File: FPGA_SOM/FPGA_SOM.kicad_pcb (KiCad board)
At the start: 6 copper layers, 42 x 38 mm, 47 parts, among them J102 Conn_01x14, J103 Conn_01x09, J104 Conn_01x11, J105 Conn_01x02, J106 Conn_01x06, U102 AP2127N-3.3, U103 W25X20CLSN, U104 AP2127N-1.2, U105 ICE40UP5K-SG48ITR, X101 ECS-2520MV-xxx-xx

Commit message: First attempt at V2. Likely to be changed in the near future.
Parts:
- removed C101, C103, C111, C123, C124, C125, C138: 100n, Capacitor_SMD:C_0603_1608Metric_Pad1.08x0.95mm_HandSolder
- removed C102, C105, C114, C126, C127, C136: 10n, Capacitor_SMD:C_0603_1608Metric_Pad1.08x0.95mm_HandSolder
- removed C116, C119, C122, C128, C137: 10u, Capacitor_SMD:C_0603_1608Metric_Pad1.08x0.95mm_HandSolder
- removed C134: 22u, Capacitor_SMD:C_0603_1608Metric_Pad1.08x0.95mm_HandSolder
- removed D101, D102, D103: LED, Diode_SMD:D_0603_1608Metric_Pad1.05x0.95mm_HandSolder
- removed D104: 1N4004, Diode_SMD:D_0603_1608Metric_Pad1.05x0.95mm_HandSolder
- removed D105, D106, D108: LED_Small, Diode_SMD:D_0603_1608Metric_Pad1.05x0.95mm_HandSolder
- removed FB101: FerriteBead, Resistor_SMD:R_1206_3216Metric
- removed J102: Conn_01x14, Connector_PinHeader_2.54mm:PinHeader_1x14_P2.54mm_Vertical
- removed J103: Conn_01x09, Connector_PinHeader_2.54mm:PinHeader_1x09_P2.54mm_Vertical
- removed J104: Conn_01x11, Connector_PinHeader_2.54mm:PinHeader_1x11_P2.54mm_Vertical
- removed J105: Conn_01x02, Connector_PinHeader_2.54mm:PinHeader_1x02_P2.54mm_Vertical
- removed J106: Conn_01x06, Connector_PinHeader_2.54mm:PinHeader_1x06_P2.54mm_Vertical
- removed R105: 100, Resistor_SMD:R_0603_1608Metric_Pad0.98x0.95mm_HandSolder
- removed R106, R109: 2k2, Resistor_SMD:R_0603_1608Metric_Pad0.98x0.95mm_HandSolder
- removed R107, R108, R111, R114: 1k, Resistor_SMD:R_0603_1608Metric_Pad0.98x0.95mm_HandSolder
- removed R110: 5k, Resistor_SMD:R_0603_1608Metric_Pad0.98x0.95mm_HandSolder
- removed R112, R113: 10k, Resistor_SMD:R_0603_1608Metric_Pad0.98x0.95mm_HandSolder
- removed U102: AP2127N-3.3, Package_TO_SOT_SMD:SOT-23
- removed U103: W25X20CLSN, Package_SO:SOIC-8_3.9x4.9mm_P1.27mm
- removed U104: AP2127N-1.2, Package_TO_SOT_SMD:SOT-23
- removed U105: ICE40UP5K-SG48ITR, Package_DFN_QFN:QFN-48-1EP_7x7mm_P0.5mm_EP5.6x5.6mm
- removed X101: ECS-2520MV-xxx-xx, Oscillator:Oscillator_SMD_ECS_2520MV-xxx-xx-4Pin_2.5x2.0mm
- added ?: VPP, TestPoint:TestPoint_Pad_2.0x2.0mm, F.Cu at (131.6, 134.6)
- added C1: 100n, Capacitor_SMD:C_0603_1608Metric, F.Cu at (131.7, 122.3)
- added C10: 100n, Capacitor_SMD:C_0603_1608Metric, F.Cu at (131.8, 130.3)
- added C11: 100n, Capacitor_SMD:C_0603_1608Metric, F.Cu at (131.8, 126.8)
- added C12: 100n, Capacitor_SMD:C_0603_1608Metric, F.Cu at (118.6, 125.2)
- added C13: 10n, Capacitor_SMD:C_0603_1608Metric, F.Cu at (131.8, 125.3)
- added C14: 10n, Capacitor_SMD:C_0603_1608Metric, F.Cu at (118.6, 123.8)
- added C15: 10u, Capacitor_SMD:C_0805_2012Metric, F.Cu at (114.5, 114.5)
- added C16: 22u, Capacitor_SMD:C_0805_2012Metric, F.Cu at (108.6, 114.5)
- added C17: 10u, Capacitor_SMD:C_0805_2012Metric, F.Cu at (125.2, 112.4)
- added C18: 100n, Capacitor_SMD:C_0603_1608Metric, F.Cu at (125.0, 114.2)
- added C19: 10n, Capacitor_SMD:C_0603_1608Metric, F.Cu at (125.0, 115.7)
- added C2: 10n, Capacitor_SMD:C_0603_1608Metric, F.Cu at (131.7, 123.8)
- added C20: 100n, Capacitor_SMD:C_0603_1608Metric, F.Cu at (123.8, 131.3)
- added C3: 100n, Capacitor_SMD:C_0603_1608Metric, F.Cu at (125.5, 131.3)
- added C4: 10n, Capacitor_SMD:C_0603_1608Metric, F.Cu at (127.0, 131.3)
- added C5: 100n, Capacitor_SMD:C_0603_1608Metric, F.Cu at (118.6, 120.8)
- added C6: 10n, Capacitor_SMD:C_0603_1608Metric, F.Cu at (118.6, 122.3)
- added C7: 10u, Capacitor_SMD:C_0805_2012Metric, F.Cu at (114.6, 108.9)
- added C8: 10u, Capacitor_SMD:C_0805_2012Metric, F.Cu at (131.9, 128.5)
- added C9: 10u, Capacitor_SMD:C_0805_2012Metric, F.Cu at (108.7, 108.9)
- added D1: 1N4004, Diode_SMD:D_0603_1608Metric, F.Cu at (128.7, 131.3)
- added D2: LED_Small, Diode_SMD:D_0603_1608Metric_Pad1.05x0.95mm_HandSolder, F.Cu at (135.9, 111.6)
- added D3: LED_Small, Diode_SMD:D_0603_1608Metric_Pad1.05x0.95mm_HandSolder, F.Cu at (135.9, 114.5)
- added D4: LED_Small, Diode_SMD:D_0603_1608Metric_Pad1.05x0.95mm_HandSolder, F.Cu at (135.9, 117.5)
- added D5: LED, Diode_SMD:D_0603_1608Metric, F.Cu at (110.9, 118.7)
- added D6: LED, Diode_SMD:D_0603_1608Metric, F.Cu at (110.9, 121.7)
- added D7: LED, Diode_SMD:D_0603_1608Metric, F.Cu at (113.0, 128.2)
- added FB1: FerriteBead, Resistor_SMD:R_1206_3216Metric, F.Cu at (125.7, 110.3)
- added J1: Conn_01x14, Connector_PinHeader_2.54mm:PinHeader_1x14_P2.54mm_Vertical, F.Cu at (147.3, 142.2)
- added J2: Conn_01x09, Connector_PinHeader_2.54mm:PinHeader_1x09_P2.54mm_Vertical, F.Cu at (134.6, 101.6)
- added J3: Conn_01x11, Connector_PinHeader_2.54mm:PinHeader_1x11_P2.54mm_Vertical, F.Cu at (116.8, 147.3)
- added J4: Conn_01x04, Connector_PinHeader_2.54mm:PinHeader_1x04_P2.54mm_Vertical, F.Cu at (104.1, 101.6)
- added J5: Conn_01x02, Connector_PinHeader_2.54mm:PinHeader_1x02_P2.54mm_Vertical, F.Cu at (113.7, 131.6)
- added J6: Conn_02x04_Counter_Clockwise, Connector_PinHeader_2.54mm:PinHeader_2x04_P2.54mm_Vertical, F.Cu at (111.8, 144.8)
- added R1: 100, Resistor_SMD:R_0603_1608Metric, F.Cu at (131.9, 131.8)
- added R10: 10k, Resistor_SMD:R_0603_1608Metric, F.Cu at (126.0, 135.3)
- added R11: 0, Resistor_SMD:R_0603_1608Metric, F.Cu at (108.7, 141.5)
- added R12: 0, Resistor_SMD:R_0603_1608Metric, F.Cu at (107.2, 141.4)
- added R2: 2k2, Resistor_SMD:R_0603_1608Metric, F.Cu at (113.9, 118.7)
- added R3: 1k, Resistor_SMD:R_0603_1608Metric, F.Cu at (132.8, 111.6)
- added R4: 1k, Resistor_SMD:R_0603_1608Metric, F.Cu at (132.8, 114.5)
- added R5: 1k, Resistor_SMD:R_0603_1608Metric, F.Cu at (132.8, 117.5)
- added R6: 1k, Resistor_SMD:R_0603_1608Metric, F.Cu at (113.9, 121.7)
- added R7: 2k2, Resistor_SMD:R_0603_1608Metric, F.Cu at (116.0, 128.2)
- added R8: 4k7, Resistor_SMD:R_0603_1608Metric, F.Cu at (116.0, 126.7)
- added R9: 10k, Resistor_SMD:R_0603_1608Metric, F.Cu at (111.2, 133.4)
- added TP10: ~{RST}, TestPoint:TestPoint_Pad_2.0x2.0mm, F.Cu at (108.3, 125.9)
- added TP11: CDN, TestPoint:TestPoint_Pad_2.0x2.0mm, F.Cu at (112.8, 124.5)
- added TP12: OSC, TestPoint:TestPoint_Pad_2.0x2.0mm, F.Cu at (134.4, 105.8)
- added TP2: VPLL, TestPoint:TestPoint_Pad_2.0x2.0mm, F.Cu at (134.7, 134.6)
- added TP3: 3V3, TestPoint:TestPoint_Pad_2.0x2.0mm, F.Cu at (142.5, 103.1)
- added TP4: 1V2, TestPoint:TestPoint_Pad_2.0x2.0mm, F.Cu at (145.5, 103.0)
- added TP5: FSS, TestPoint:TestPoint_Pad_2.0x2.0mm, F.Cu at (108.3, 134.3)
- added TP6: ISS, TestPoint:TestPoint_Pad_2.0x2.0mm, F.Cu at (108.3, 130.2)
- added TP7: SCK, TestPoint:TestPoint_Pad_2.0x2.0mm, F.Cu at (103.5, 141.2)
- added TP8: SDO, TestPoint:TestPoint_Pad_2.0x2.0mm, F.Cu at (115.3, 138.3)
- added TP9: SDI, TestPoint:TestPoint_Pad_2.0x2.0mm, F.Cu at (111.4, 138.4)
- added U1: ICE40UP5K-SG48ITR, Package_DFN_QFN:QFN-48-1EP_7x7mm_P0.5mm_EP5.6x5.6mm, F.Cu at (125.0, 125.0)
- added U2: AP2127N-3.3, Package_TO_SOT_SMD:SOT-23, F.Cu at (111.6, 108.9)
- added U3: AP2127N-1.2, Package_TO_SOT_SMD:SOT-23, F.Cu at (111.6, 114.5)
- added U4: W25X20CLSN, Package_SO:SOIC-8_3.9x4.9mm_P1.27mm, F.Cu at (119.3, 132.9)
- added X1: ECS-2520MV-xxx-xx, Oscillator:Oscillator_SMD_ECS_2520MV-xxx-xx-4Pin_2.5x2.0mm, F.Cu at (125.2, 117.9)
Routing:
- net Net-(J104-Pin_2): track 33.0 -> 0.00 mm, vias 1 -> 0
- net Net-(J104-Pin_10): track 31.2 -> 0.00 mm, vias 1 -> 0
- net Net-(J104-Pin_1): track 30.0 -> 0.00 mm
- net Net-(J104-Pin_9): track 29.9 -> 0.00 mm, vias 1 -> 0
- net Net-(J1-Pin_14): track 0.00 -> 29.4 mm, vias 0 -> 1
- net Net-(J1-Pin_1): track 0.00 -> 27.5 mm, vias 0 -> 1
- net Net-(J1-Pin_13): track 0.00 -> 26.7 mm, vias 0 -> 1
- net Net-(J104-Pin_7): track 26.6 -> 0.00 mm, vias 1 -> 0
- net Net-(J102-Pin_14): track 26.2 -> 0.00 mm
- net Net-(J3-Pin_11): track 0.00 -> 26.0 mm, vias 0 -> 1
- net Net-(J2-Pin_8): track 0.00 -> 25.8 mm, vias 0 -> 1
- net Net-(J104-Pin_8): track 25.8 -> 0.00 mm, vias 1 -> 0
- net /CDONE: track 9.61 -> 35.2 mm, vias 0 -> 1
- net Net-(J3-Pin_10): track 0.00 -> 25.3 mm, vias 0 -> 1
- net Net-(J1-Pin_2): track 0.00 -> 25.1 mm, vias 0 -> 1
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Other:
- board size 42 x 38 mm -> 50 x 50 mm
- board text added: "*"
- board text added: "10"
- board text added: "11"
- board text added: "12"
- board text added: "19"
- board text added: "1V"
- board text added: "1V2"
- board text added: "21"
- board text added: "26"
- board text added: "27"
- board text added: "28"
- board text added: "3"
- board text added: "32"
- board text added: "34"
- board text added: "35"
- board text added: "3V"
- board text added: "47"
- board text added: "CD"
- board text added: "CS"
- board text added: "GD"
- board text added: "SCK"
- board text added: "SDI"
- board text added: "SDO"
- board text removed: "0"
- board text removed: "16"
- board text removed: "22"
- board text removed: "24"
- board text removed: "29"
- board text removed: "3/G6"
- board text removed: "38x42mm Designed by Tobias McKellar V1.0"
- board text removed: "39"
- board text removed: "41"
- board text removed: "44"
- board text removed: "49"
- board text removed: "5"
- board text removed: "50"
- board text removed: "51"
- board text removed: "8"
- board text removed: "CK"
- board text removed: "JLCJLCJLCJLC"
- board text removed: "MIS"
- board text removed: "MOS"
- board text removed: "SS"

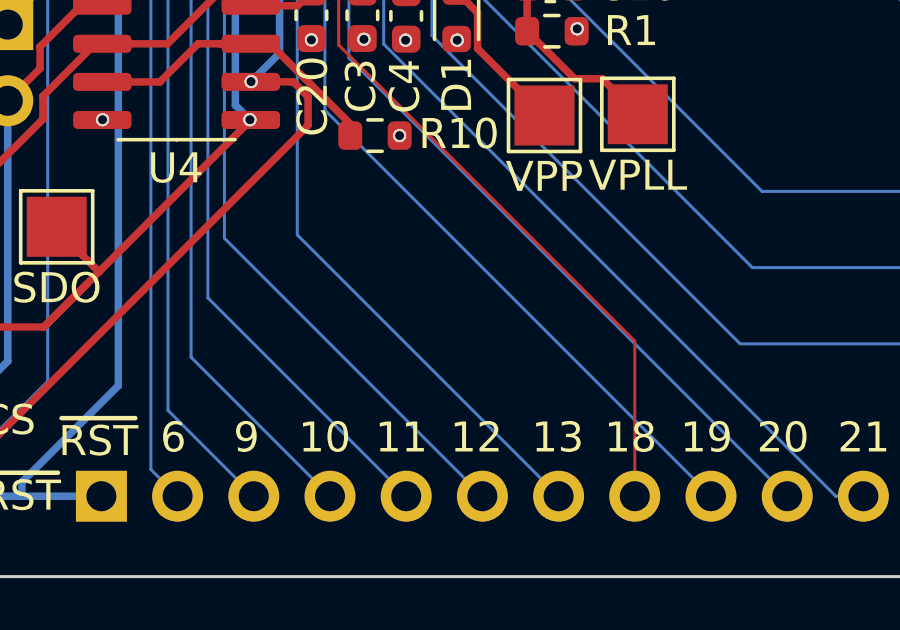
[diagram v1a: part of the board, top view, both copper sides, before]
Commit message: Added JLC text and my name. to silkscreen.
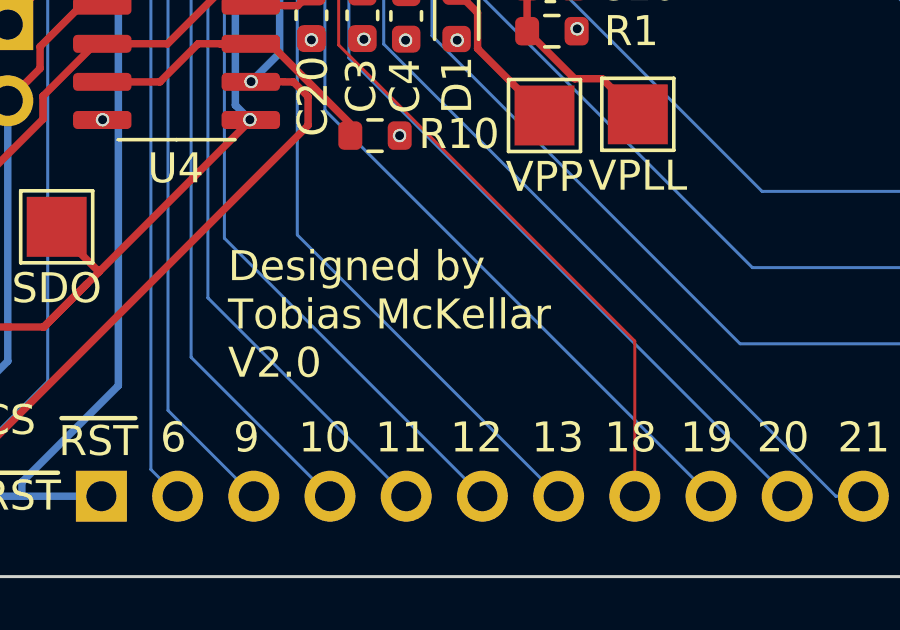
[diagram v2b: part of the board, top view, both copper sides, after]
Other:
- board text added: "Designed by Tobias McKellar V2.0"
- board text added: "JLCJLCJLCJLC"
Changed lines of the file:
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@@
   (gr_rect locked (start 100 100) (end 150 150)
     (stroke (width 0.1) (type default)) (fill none) (layer "Edge.Cuts"))
+  (gr_text "JLCJLCJLCJLC" (at 134.6 149.51) (layer "B.SilkS")
+    (effects (font (size 1 1) (thickness 0.15)) (justify left bottom mirror))
+  )
+  (gr_text "Designed by \nTobias McKellar\nV2.0" (at 121.06 143.46) (layer "F.SilkS")
+    (effects (font (size 1 1) (thickness 0.15)) (justify left bottom))
+  )
   (gr_text "28" (at 143.7 132.51) (layer "F.SilkS")
     (effects (font (size 1 1) (thickness 0.15)) (justify left bottom))

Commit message: Saving progress.
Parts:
- removed ?: VPP, TestPoint:TestPoint_Pad_2.0x2.0mm
- removed D1: 1N4004, Diode_SMD:D_0603_1608Metric
- removed D6: LED, Diode_SMD:D_0603_1608Metric
- removed J4: Conn_01x04, Connector_PinHeader_2.54mm:PinHeader_1x04_P2.54mm_Vertical
- removed J6: Conn_02x04_Counter_Clockwise, Connector_PinHeader_2.54mm:PinHeader_2x04_P2.54mm_Vertical
- removed R12: 0, Resistor_SMD:R_0603_1608Metric
- removed TP2: VPLL, TestPoint:TestPoint_Pad_2.0x2.0mm
- added H1: MountingHole, MountingHole:MountingHole_3.2mm_M3, F.Cu at (104.1, 104.1)
- added H2: MountingHole, MountingHole:MountingHole_3.2mm_M3, F.Cu at (147.3, 104.1)
- added H3: MountingHole, MountingHole:MountingHole_3.2mm_M3, F.Cu at (147.3, 144.8)
- added H4: MountingHole, MountingHole:MountingHole_3.2mm_M3, F.Cu at (104.1, 144.8)
- added J7: Conn_01x09, Connector_PinHeader_2.54mm:PinHeader_1x09_P2.54mm_Vertical, F.Cu at (147.3, 137.2)
- added J8: Conn_01x10, Connector_PinHeader_2.54mm:PinHeader_1x10_P2.54mm_Vertical, F.Cu at (101.6, 114.3)
- added R13: 0, Resistor_SMD:R_0603_1608Metric, F.Cu at (123.5, 131.5)
- added TP1: VPLL, TestPoint:TestPoint_Pad_2.0x2.0mm, B.Cu at (131.8, 130.6)
- C1, C11, C12, C20, C3, C5, R1, R10, R8: moved to B.Cu
- C16: value 22u -> 10u
- C8: value 10u -> 4.7u; footprint Capacitor_SMD:C_0805_2012Metric -> Capacitor_SMD:C_0603_1608Metric; moved to B.Cu
- J1: value Conn_01x14 -> Conn_01x12; footprint Connector_PinHeader_2.54mm:PinHeader_1x14_P2.54mm_Vertical -> Connector_PinHeader_2.54mm:PinHeader_1x12_P2.54mm_Vertical
- J2: value Conn_01x09 -> Conn_02x05_Counter_Clockwise; footprint Connector_PinHeader_2.54mm:PinHeader_1x09_P2.54mm_Vertical -> Connector_PinHeader_2.54mm:PinHeader_2x05_P2.54mm_Vertical
- J3: value Conn_01x11 -> Conn_01x06; footprint Connector_PinHeader_2.54mm:PinHeader_1x11_P2.54mm_Vertical -> Connector_PinHeader_2.54mm:PinHeader_1x06_P2.54mm_Vertical
- R11: value 0 -> 10k
- R3, R4: value 1k -> 10k; moved to B.Cu
- R5: value 1k -> 10k
- R6: value 1k -> 0
- moved J2 52.5 mm to (109.5, 147.8), turned to 90 degrees
- moved J1 38.9 mm to (139.7, 104.1), turned to -90 degrees
- moved D5 31.1 mm to (140.9, 110.3), turned to 90 degrees
- moved R2 29.7 mm to (142.4, 110.4), turned to 90 degrees
- moved R3 26.9 mm to (127.1, 138.0)
- moved TP7 22.9 mm to (126.3, 141.5), turned to 0 degrees
- moved R4 22.7 mm to (127.1, 136.5)
- moved R11 16.9 mm to (119.3, 128.3), turned to 0 degrees
- moved R5 16.4 mm to (118.6, 125.7), turned to 0 degrees
- moved R6 14.9 mm to (123.5, 133.1)
- moved TP12 14.5 mm to (126.5, 118.0), turned to 90 degrees
- moved R7 14.0 mm to (111.9, 141.6), turned to 90 degrees
- moved D7 13.6 mm to (110.4, 141.6), turned to -90 degrees
- moved TP5 8.62 mm to (116.9, 133.6), turned to -90 degrees
- moved TP8 8.56 mm to (123.3, 141.5)
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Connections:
- net Net-(X1-Tri-State) renamed /V_OSC
- D2 pad 1: Net-(D2-K) -> /RGB0
- D3 pad 1: Net-(D3-K) -> /RGB1
- D4 pad 1: Net-(D4-K) -> /RGB2
- J1 pad 1: Net-(J1-Pin_1) -> /37_G1
- J1 pad 10: Net-(J1-Pin_10) -> GND
- J1 pad 11: Net-(J1-Pin_11) -> /3V3
- J1 pad 12: Net-(J1-Pin_12) -> +5V
- J1 pad 2: Net-(J1-Pin_2) -> /38
- J1 pad 3: Net-(J1-Pin_3) -> /42
- J1 pad 4: Net-(J1-Pin_4) -> /43
- J1 pad 5: Net-(J1-Pin_5) -> /CLK_IN_G6
- J1 pad 6: Net-(J1-Pin_6) -> /45
- J1 pad 7: Net-(J1-Pin_7) -> /DP1_N
- J1 pad 8: Net-(J1-Pin_8) -> /DP1_P
- J1 pad 9: Net-(J1-Pin_9) -> /48
- J2 pad 1: /FPGA_OSCILLATOR -> /FLASH_SS
- J2 pad 2: Net-(J2-Pin_2) -> /FLASH_DO
- J2 pad 3: Net-(J2-Pin_3) -> /FLASH_DI
- J2 pad 4: Net-(J2-Pin_4) -> /SCK
- J2 pad 5: Net-(J2-Pin_5) -> unconnected-(J2-Pin_5-Pad5)
- J2 pad 6: Net-(J2-Pin_6) -> unconnected-(J2-Pin_6-Pad6)
- J2 pad 7: Net-(J2-Pin_7) -> GND
- J2 pad 8: Net-(J2-Pin_8) -> /3V3
- J2 pad 9: +5V -> /CDONE
- J3 pad 1: /CRESET -> /13
- J3 pad 2: Net-(J3-Pin_2) -> /18
- J3 pad 3: Net-(J3-Pin_3) -> /19
- J3 pad 4: Net-(J3-Pin_4) -> /20
- J3 pad 5: Net-(J3-Pin_5) -> /21
- J3 pad 6: Net-(J3-Pin_6) -> /23
- R10 pad 2: Net-(U4-~{HOLD}) -> Net-(U4-~{WP})
- R11 pad 1: /FLASH_MISO -> /3V3
- R11 pad 2: Net-(J6-Pin_2) -> /ICE_SS
- R3 pad 1: Net-(D2-K) -> /3V3
- R3 pad 2: Net-(U1A-RGB2) -> /SCK
- R4 pad 1: Net-(D3-K) -> /3V3
- R4 pad 2: Net-(U1A-RGB1) -> Net-(U4-~{HOLD})
- R5 pad 1: Net-(D4-K) -> /3V3
- R5 pad 2: Net-(U1A-RGB0) -> /CRESET
- R6 pad 1: /1V2 -> /FLASH_DI
- R6 pad 2: Net-(D6-A) -> Net-(U1B-IOB_32a_SPI_SO)
- TP12 pad 1: /FPGA_OSCILLATOR -> /CLK_IN_G6
- TP8 pad 1: /FLASH_MOSI -> /FLASH_DI
- TP9 pad 1: /FLASH_MISO -> /FLASH_DO
- U1 pad 10: Net-(J3-Pin_4) -> /10
- U1 pad 11: Net-(J3-Pin_5) -> /11
- U1 pad 12: Net-(J3-Pin_6) -> /12
- U1 pad 13: Net-(J3-Pin_7) -> /13
- U1 pad 14: /FLASH_MOSI -> Net-(U1B-IOB_32a_SPI_SO)
- U1 pad 17: /FLASH_MISO -> Net-(U1B-IOB_33b_SPI_SI)
- U1 pad 18: Net-(J3-Pin_8) -> /18
- U1 pad 19: Net-(J3-Pin_9) -> /19
- U1 pad 2: Net-(J2-Pin_6) -> /2
- U1 pad 20: Net-(J3-Pin_10) -> /20
- U1 pad 21: Net-(J3-Pin_11) -> /21
- U1 pad 23: Net-(J1-Pin_1) -> /23
- U1 pad 24: Net-(D1-K) -> /3V3
- U1 pad 25: Net-(J1-Pin_2) -> /25
- U1 pad 26: Net-(J1-Pin_3) -> /26
- U1 pad 27: Net-(J1-Pin_4) -> /27
- U1 pad 28: Net-(J1-Pin_5) -> /28
- U1 pad 3: Net-(J2-Pin_7) -> /3
- U1 pad 31: Net-(J1-Pin_6) -> /RDP_N
- U1 pad 32: Net-(J1-Pin_7) -> /RDP_P
- U1 pad 34: Net-(J1-Pin_8) -> /34
- U1 pad 35: Net-(J1-Pin_9) -> /35_G0
- U1 pad 36: Net-(J1-Pin_10) -> /36
- U1 pad 37: Net-(J1-Pin_11) -> /37_G1
- U1 pad 38: Net-(J1-Pin_12) -> /38
- U1 pad 39: Net-(U1A-RGB0) -> /RGB0
- U1 pad 4: Net-(J2-Pin_8) -> /4
- U1 pad 40: Net-(U1A-RGB1) -> /RGB1
- U1 pad 41: Net-(U1A-RGB2) -> /RGB2
- U1 pad 42: Net-(J1-Pin_13) -> /42
- U1 pad 43: Net-(J1-Pin_14) -> /43
- U1 pad 44: /FPGA_OSCILLATOR -> /CLK_IN_G6
- U1 pad 45: Net-(J2-Pin_2) -> /45
- U1 pad 46: Net-(J2-Pin_3) -> /DP1_N
- U1 pad 47: Net-(J2-Pin_4) -> /DP1_P
- U1 pad 48: Net-(J2-Pin_5) -> /48
- U1 pad 6: Net-(J3-Pin_2) -> /6
- U1 pad 9: Net-(J3-Pin_3) -> /9
- U4 pad 2: /FLASH_MISO -> /FLASH_DO
- U4 pad 3: Net-(U4-~{HOLD}) -> Net-(U4-~{WP})
- U4 pad 5: /FLASH_MOSI -> /FLASH_DI
- X1 pad 3: /FPGA_OSCILLATOR -> /CLK_IN_G6
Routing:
- net Net-(J1-Pin_14): track 29.4 -> 0.00 mm, vias 1 -> 0
- net /FLASH_MOSI: track 29.0 -> 0.00 mm, vias 2 -> 0
- net Net-(J1-Pin_1): track 27.5 -> 0.00 mm, vias 1 -> 0
- net Net-(J1-Pin_13): track 26.7 -> 0.00 mm, vias 1 -> 0
- net /FPGA_OSCILLATOR: track 26.2 -> 0.00 mm
- net Net-(J3-Pin_11): track 26.0 -> 0.00 mm, vias 1 -> 0
- net Net-(J2-Pin_8): track 25.8 -> 0.00 mm, vias 1 -> 0
- net Net-(J3-Pin_10): track 25.3 -> 0.00 mm, vias 1 -> 0
- net /37_G1: track 0.00 -> 25.2 mm, vias 0 -> 1
- net Net-(J1-Pin_2): track 25.1 -> 0.00 mm, vias 1 -> 0
- net Net-(J3-Pin_2): track 24.8 -> 0.00 mm, vias 1 -> 0
- net Net-(J3-Pin_9): track 24.6 -> 0.00 mm, vias 1 -> 0
- net Net-(J3-Pin_7): track 24.4 -> 0.00 mm, vias 1 -> 0
- net Net-(J3-Pin_3): track 24.3 -> 0.00 mm, vias 1 -> 0
- net Net-(J2-Pin_7): track 24.2 -> 0.00 mm, vias 1 -> 0
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- added copper zone on F.Cu, net /V_OSC
- removed copper zone on F.Cu, net +5V
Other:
- board text removed: "*"
- board text removed: "10"
- board text removed: "11"
- board text removed: "12"
- board text removed: "13"
- board text removed: "18"
- board text removed: "19"
- board text removed: "1V"
- board text removed: "1V2"
- board text removed: "2"
- board text removed: "20"
- board text removed: "21"
- board text removed: "23"
- board text removed: "25"
- board text removed: "26"
- board text removed: "27"
- board text removed: "28"
- board text removed: "3"
- board text removed: "31"
- board text removed: "32"
- board text removed: "34"
- board text removed: "35"
- board text removed: "36"
- board text removed: "37"
- board text removed: "38"
- board text removed: "3V"
- board text removed: "3V3"
- board text removed: "4"
- board text removed: "42"
- board text removed: "43"
- board text removed: "45"
- board text removed: "46"
- board text removed: "47"
- board text removed: "48"
- board text removed: "5V"
- board text removed: "6"
- board text removed: "9"
- board text removed: "CD"
- board text removed: "CS"
- board text removed: "Designed by Tobias McKellar V2.0"
- board text removed: "GD"
- board text removed: "GND"
- board text removed: "JLCJLCJLCJLC"
- board text removed: "SCK"
- board text removed: "SDI"
- board text removed: "SDO"
- board text removed: "~{RST}"

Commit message: Remove some unnecessary capacitors and resize others.
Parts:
- removed C14, C4, C6: 10n, Capacitor_SMD:C_0603_1608Metric
- C13, C2: value 10n -> 4.7u
- C15, C16, C9: value 10u -> 1u
- C5: moved to F.Cu

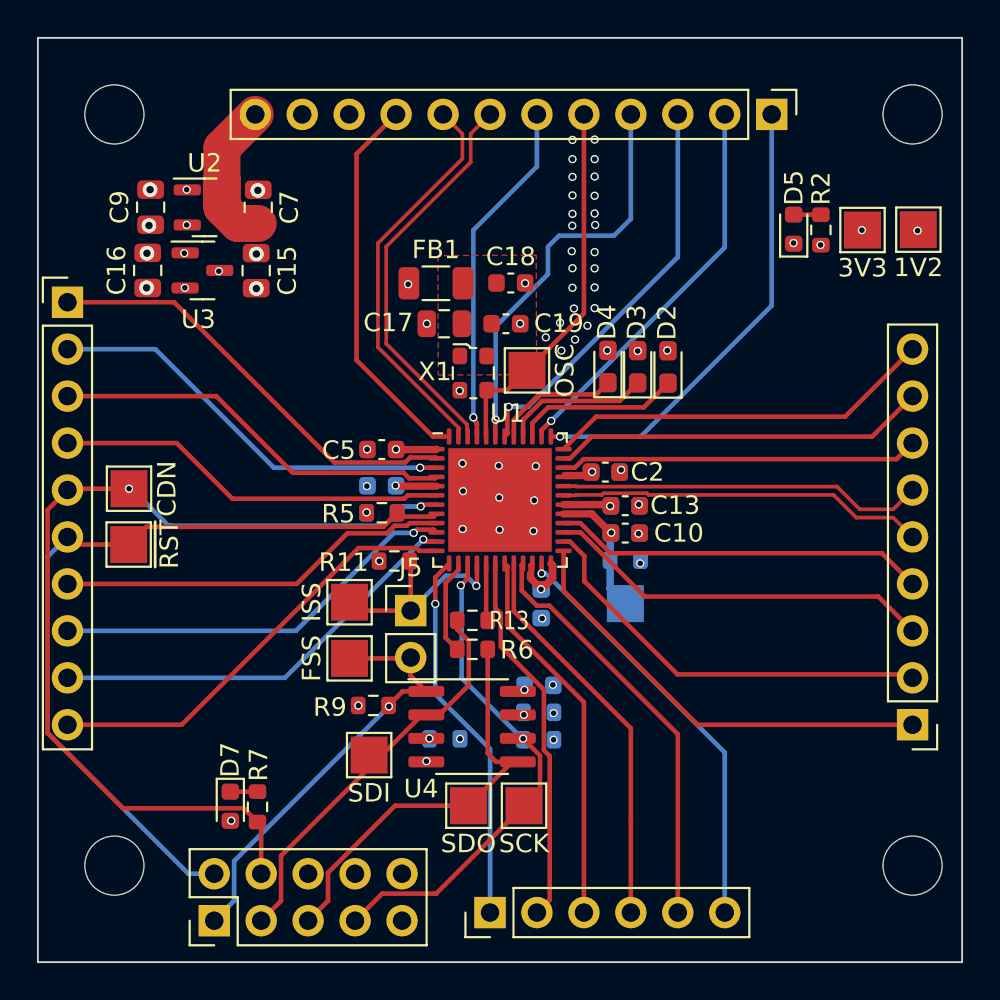
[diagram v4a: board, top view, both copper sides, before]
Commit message: Added silkscreen and removed unneded test points.
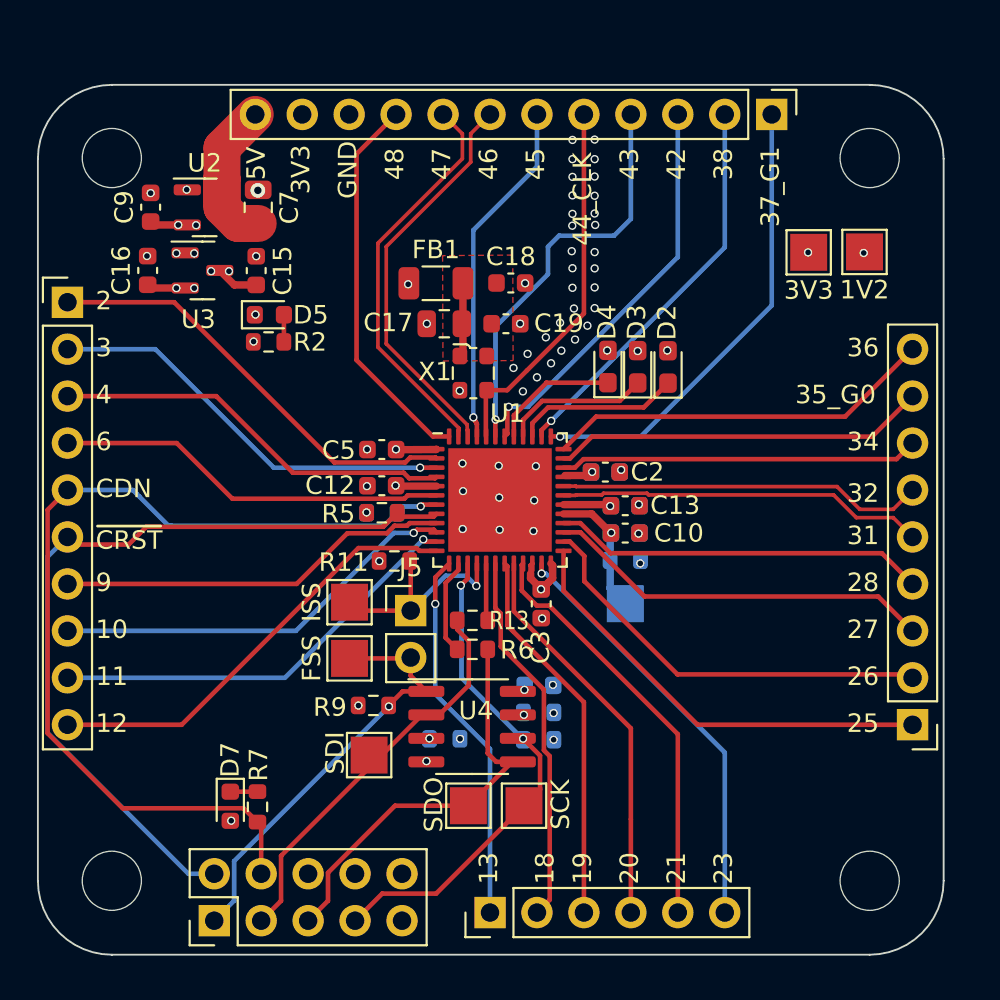
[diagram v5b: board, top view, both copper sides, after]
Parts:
- removed TP10: ~{RST}, TestPoint:TestPoint_Pad_2.0x2.0mm
- removed TP11: CDN, TestPoint:TestPoint_Pad_2.0x2.0mm
- removed TP12: OSC, TestPoint:TestPoint_Pad_2.0x2.0mm
- C12, C3: moved to F.Cu
- C15, C16, C9: footprint Capacitor_SMD:C_0805_2012Metric -> Capacitor_SMD:C_0603_1608Metric
- moved R2 30.5 mm to (112.5, 116.4), turned to 0 degrees
- moved D5 28.7 mm to (112.5, 115.0), turned to 0 degrees
- moved H2 3.31 mm to (145.0, 106.5)
- moved TP3 3.15 mm to (141.7, 111.6)
- moved TP4 3.15 mm to (144.7, 111.6)
- moved H3 2.46 mm to (145.0, 145.6)
- moved H1 2.36 mm to (104.0, 106.5)
- moved H4 0.83 mm to (104.0, 145.6)
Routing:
- net /3V3: track 9.10 -> 13.5 mm
- net /V_OSC: track 0.00 -> 4.00 mm
- net /1V2: track 4.78 -> 6.88 mm
- net /CDONE: track 52.3 -> 51.2 mm, vias 2 -> 1
- net GND: vias 53 -> 54
- net (no net): vias 0 -> 5
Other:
- board size 50 x 50 mm -> 49 x 47.1 mm
- board text added: "10"
- board text added: "11"
- board text added: "12"
- board text added: "13"
- board text added: "18"
- board text added: "19"
- board text added: "2"
- board text added: "20"
- board text added: "21"
- board text added: "23"
- board text added: "25"
- board text added: "26"
- board text added: "27"
- board text added: "28"
- board text added: "3"
- board text added: "31"
- board text added: "32"
- board text added: "34"
- board text added: "35_G0"
- board text added: "36"
- board text added: "37_G1"
- board text added: "38"
- board text added: "3V3"
- board text added: "4"
- board text added: "42"
- board text added: "43"
- board text added: "44_CLK"
- board text added: "45"
- board text added: "46"
- board text added: "47"
- board text added: "48"
- board text added: "5V"
- board text added: "6"
- board text added: "9"
- board text added: "CDN"
- board text added: "GND"
- board text added: "~{CRST}"

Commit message: ficing small things and adding qr code to repo.
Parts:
- moved R11 8.11 mm to (113.3, 133.8), turned to 90 degrees
- moved D5 2.06 mm to (113.9, 116.5)
- moved R2 2.06 mm to (113.8, 118.0)
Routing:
- net /ICE_SS: track 12.0 -> 15.1 mm
- net /3V3: track 13.5 -> 14.9 mm
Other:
- board text added: "Git Repo"
- board text added: "NC GND 3V3 CDN ~{CRST} NC SCK FDI FDO FSS"
